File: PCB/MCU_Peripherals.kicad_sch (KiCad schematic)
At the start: 44 parts, among them IC3 LAN8742A-CZ-TR, IC4 USBLC6-4SC6, IC6 USBLC6-4SC6, J3 USB4216-03-A, J6 SS-90000-009, T1 H1102NL

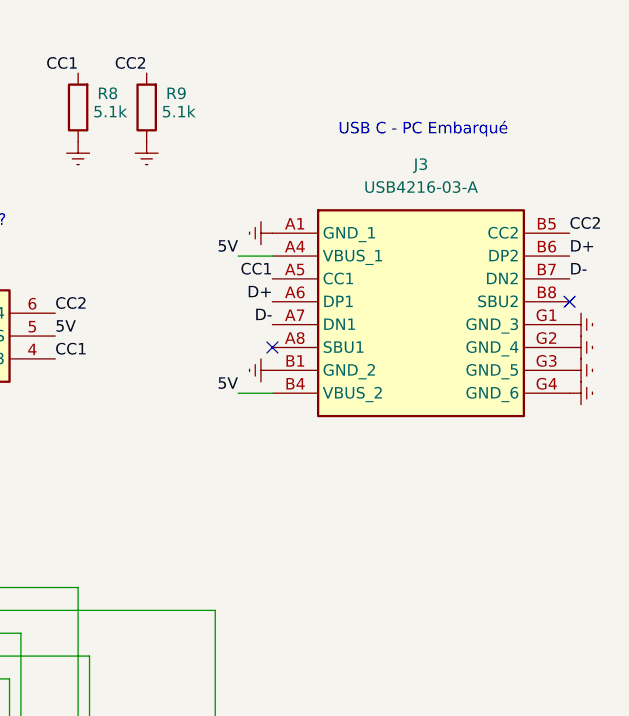
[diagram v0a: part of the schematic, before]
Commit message: Updated a lot of stuff:
Added encoders,
Added 5V power supply for actuators
Added 12V power supply for actuators
Renamed sheets to be clearer
Added usb debug
Modify MCU sheet to be A3 format
Linked some pins
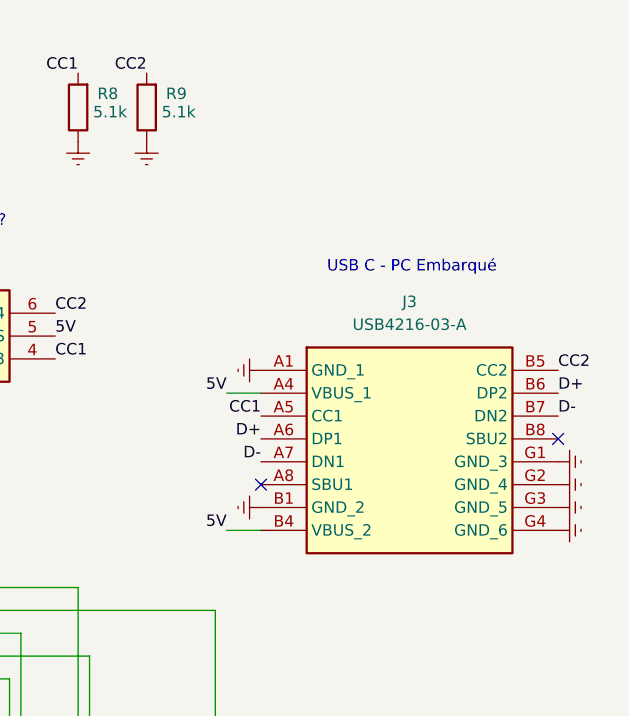
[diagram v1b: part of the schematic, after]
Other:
- moved on the sheet: J3
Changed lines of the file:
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@@
 	(text "USB C - PC Embarqué"
 		(exclude_from_sim no)
-		(at 258.064 26.67 0)
+		(at 256.794 41.91 0)
 		(effects
 			(font
@@
 	)
 	(no_connect
-		(at 241.3 50.8)
+		(at 240.03 66.04)
 	)
 	(no_connect
-		(at 274.32 45.72)
+		(at 273.05 60.96)
 	)
 	(no_connect
@@
 	(wire
 		(pts
-			(xy 237.49 40.64) (xy 241.3 40.64)
+			(xy 236.22 55.88) (xy 240.03 55.88)
 		)
 		(stroke
@@
 	(wire
 		(pts
-			(xy 237.49 55.88) (xy 241.3 55.88)
+			(xy 236.22 71.12) (xy 240.03 71.12)
 		)
 		(stroke
@@
 	)
 	(label "D-"
-		(at 274.32 43.18 0)
+		(at 273.05 58.42 0)
 		(effects
 			(font
@@
 	)
 	(label "CC2"
-		(at 274.32 38.1 0)
+		(at 273.05 53.34 0)
 		(effects
 			(font
@@
 	)
 	(label "5V"
-		(at 237.49 55.88 180)
+		(at 236.22 71.12 180)
 		(effects
 			(font
@@
 	)
 	(label "CC1"
-		(at 241.3 43.18 180)
+		(at 240.03 58.42 180)
 		(effects
 			(font
@@
 	)
 	(label "D+"
-		(at 241.3 45.72 180)
+		(at 240.03 60.96 180)
 		(effects
 			(font
@@
 	)
 	(label "D+"
-		(at 274.32 40.64 0)
+		(at 273.05 55.88 0)
 		(effects
 			(font
@@
 	)
 	(label "5V"
-		(at 237.49 40.64 180)
+		(at 236.22 55.88 180)
 		(effects
 			(font
@@
 	)
 	(label "D-"
-		(at 241.3 48.26 180)
+		(at 240.03 63.5 180)
 		(effects
 			(font
@@
 	(symbol
 		(lib_id "power:GNDREF")
-		(at 274.32 55.88 90)
+		(at 273.05 71.12 90)
 		(unit 1)
 		(exclude_from_sim no)
@@
 		(fields_autoplaced yes)
 		(property "Reference" "#PWR043"
-			(at 280.67 55.88 0)
+			(at 279.4 71.12 0)
 			(effects
 				(font
@@
 		)
 		(property "Value" "GNDREF"
-			(at 278.13 55.8799 90)
+			(at 276.86 71.1199 90)
 			(effects
 				(font
@@
 		)
 		(property "Footprint" ""
-			(at 274.32 55.88 0)
+			(at 273.05 71.12 0)
 			(effects
 				(font
@@
 		)
 		(property "Datasheet" ""
-			(at 274.32 55.88 0)
+			(at 273.05 71.12 0)
 			(effects
 				(font
@@
 		)
 		(property "Description" "Power symbol creates a global label with name \"GNDREF\" , reference supply ground"
-			(at 274.32 55.88 0)
+			(at 273.05 71.12 0)
 			(effects
 				(font
@@
 	(symbol
 		(lib_id "power:GNDREF")
-		(at 274.32 48.26 90)
+		(at 273.05 63.5 90)
 		(unit 1)
 		(exclude_from_sim no)
@@
 		(fields_autoplaced yes)
 		(property "Reference" "#PWR037"
-			(at 280.67 48.26 0)
+			(at 279.4 63.5 0)
 			(effects
 				(font
@@
 		)
 		(property "Value" "GNDREF"
-			(at 278.13 48.2599 90)
+			(at 276.86 63.4999 90)
 			(effects
 				(font
@@
 		)
 		(property "Footprint" ""
-			(at 274.32 48.26 0)
+			(at 273.05 63.5 0)
 			(effects
 				(font
@@
 		)
 		(property "Datasheet" ""
-			(at 274.32 48.26 0)
+			(at 273.05 63.5 0)
 			(effects
 				(font
@@
 		)
 		(property "Description" "Power symbol creates a global label with name \"GNDREF\" , reference supply ground"
-			(at 274.32 48.26 0)
+			(at 273.05 63.5 0)
 			(effects
 				(font
@@
 	(symbol
 		(lib_id "power:GNDREF")
-		(at 241.3 38.1 270)
+		(at 240.03 53.34 270)
 		(unit 1)
 		(exclude_from_sim no)
@@
 		(fields_autoplaced yes)
 		(property "Reference" "#PWR048"
-			(at 234.95 38.1 0)
+			(at 233.68 53.34 0)
 			(effects
 				(font
@@
 		)
 		(property "Value" "GNDREF"
-			(at 237.49 38.1001 90)
+			(at 236.22 53.3401 90)
 			(effects
 				(font
@@
 		)
 		(property "Footprint" ""
-			(at 241.3 38.1 0)
+			(at 240.03 53.34 0)
 			(effects
 				(font
@@
 		)
 		(property "Datasheet" ""
-			(at 241.3 38.1 0)
+			(at 240.03 53.34 0)
 			(effects
 				(font
@@
 		)
 		(property "Description" "Power symbol creates a global label with name \"GNDREF\" , reference supply ground"
-			(at 241.3 38.1 0)
+			(at 240.03 53.34 0)
 			(effects
 				(font
@@
 	(symbol
 		(lib_id "power:GNDREF")
-		(at 274.32 53.34 90)
+		(at 273.05 68.58 90)
 		(unit 1)
 		(exclude_from_sim no)
@@
 		(fields_autoplaced yes)
 		(property "Reference" "#PWR042"
-			(at 280.67 53.34 0)
+			(at 279.4 68.58 0)
 			(effects
 				(font
@@
 		)
 		(property "Value" "GNDREF"
-			(at 278.13 53.3399 90)
+			(at 276.86 68.5799 90)
 			(effects
 				(font
@@
 		)
 		(property "Footprint" ""
-			(at 274.32 53.34 0)
+			(at 273.05 68.58 0)
 			(effects
 				(font
@@
 		)
 		(property "Datasheet" ""
-			(at 274.32 53.34 0)
+			(at 273.05 68.58 0)
 			(effects
 				(font
@@
 		)
 		(property "Description" "Power symbol creates a global label with name \"GNDREF\" , reference supply ground"
-			(at 274.32 53.34 0)
+			(at 273.05 68.58 0)
 			(effects
 				(font
@@
 	(symbol
 		(lib_id "power:GNDREF")
-		(at 241.3 53.34 270)
+		(at 240.03 68.58 270)
 		(unit 1)
 		(exclude_from_sim no)
@@
 		(fields_autoplaced yes)
 		(property "Reference" "#PWR047"
-			(at 234.95 53.34 0)
+			(at 233.68 68.58 0)
 			(effects
 				(font
@@
 		)
 		(property "Value" "GNDREF"
-			(at 237.49 53.3401 90)
+			(at 236.22 68.5801 90)
 			(effects
 				(font
@@
 		)
 		(property "Footprint" ""
-			(at 241.3 53.34 0)
+			(at 240.03 68.58 0)
 			(effects
 				(font
@@
 		)
 		(property "Datasheet" ""
-			(at 241.3 53.34 0)
+			(at 240.03 68.58 0)
 			(effects
 				(font
@@
 		)
 		(property "Description" "Power symbol creates a global label with name \"GNDREF\" , reference supply ground"
-			(at 241.3 53.34 0)
+			(at 240.03 68.58 0)
 			(effects
 				(font
@@
 	(symbol
 		(lib_id "SamacSys_Parts:USB4216-03-A")
-		(at 241.3 38.1 0)
+		(at 240.03 53.34 0)
 		(unit 1)
 		(exclude_from_sim no)
@@
 		(fields_autoplaced yes)
 		(property "Reference" "J3"
-			(at 257.81 30.48 0)
+			(at 256.54 45.72 0)
 			(effects
 				(font
@@
 		)
 		(property "Value" "USB4216-03-A"
-			(at 257.81 33.02 0)
+			(at 256.54 48.26 0)
 			(effects
 				(font
@@
 		)
 		(property "Footprint" "USB421603A"
-			(at 270.51 133.02 0)
+			(at 269.24 148.26 0)
 			(effects
 				(font
@@
 		)
 		(property "Datasheet" "https://eu.mouser.com/datasheet/2/837/usb4216-3577180.pdf"
-			(at 270.51 233.02 0)
+			(at 269.24 248.26 0)
 			(effects
 				(font
@@
 		)
 		(property "Description" "USB Connectors USB C Receptacle, Short Body, USB2.0, 16Pin, Horizontal, SMT"
-			(at 241.3 38.1 0)
+			(at 240.03 53.34 0)
 			(effects
 				(font
@@
 		)
 		(property "Height" ""
-			(at 270.51 433.02 0)
+			(at 269.24 448.26 0)
 			(effects
 				(font
@@
 		)
 		(property "Manufacturer_Name" "GCT (GLOBAL CONNECTOR TECHNOLOGY)"
-			(at 270.51 533.02 0)
+			(at 269.24 548.26 0)
 			(effects
 				(font
@@
 		)
 		(property "Manufacturer_Part_Number" "USB4216-03-A"
-			(at 270.51 633.02 0)
+			(at 269.24 648.26 0)
 			(effects
 				(font
@@
 		)
 		(property "Mouser Part Number" "640-USB4216-03-A"
-			(at 270.51 733.02 0)
+			(at 269.24 748.26 0)
 			(effects
 				(font
@@
 		)
 		(property "Mouser Price/Stock" "https://www.mouser.co.uk/ProductDetail/GCT/USB4216-03-A?qs=Tc%252BHE9vUsnv1G2UWLFIexA%3D%3D"
-			(at 270.51 833.02 0)
+			(at 269.24 848.26 0)
 			(effects
 				(font
@@
 		)
 		(property "Arrow Part Number" ""
-			(at 270.51 933.02 0)
+			(at 269.24 948.26 0)
 			(effects
 				(font
@@
 		)
 		(property "Arrow Price/Stock" ""
-			(at 270.51 1033.02 0)
+			(at 269.24 1048.26 0)
 			(effects
 				(font
@@
 	(symbol
 		(lib_id "power:GNDREF")
-		(at 274.32 50.8 90)
+		(at 273.05 66.04 90)
 		(unit 1)
 		(exclude_from_sim no)
@@
 		(fields_autoplaced yes)
 		(property "Reference" "#PWR038"
-			(at 280.67 50.8 0)
+			(at 279.4 66.04 0)
 			(effects
 				(font
@@
 		)
 		(property "Value" "GNDREF"
-			(at 278.13 50.7999 90)
+			(at 276.86 66.0399 90)
 			(effects
 				(font
@@
 		)
 		(property "Footprint" ""
-			(at 274.32 50.8 0)
+			(at 273.05 66.04 0)
 			(effects
 				(font
@@
 		)
 		(property "Datasheet" ""
-			(at 274.32 50.8 0)
+			(at 273.05 66.04 0)
 			(effects
 				(font
@@
 		)
 		(property "Description" "Power symbol creates a global label with name \"GNDREF\" , reference supply ground"
-			(at 274.32 50.8 0)
+			(at 273.05 66.04 0)
 			(effects
 				(font
